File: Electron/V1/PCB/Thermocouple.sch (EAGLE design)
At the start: 30 parts, among them U1 MAX31855K, U2 ELECTRONDUALNAMED, U3 24LC512

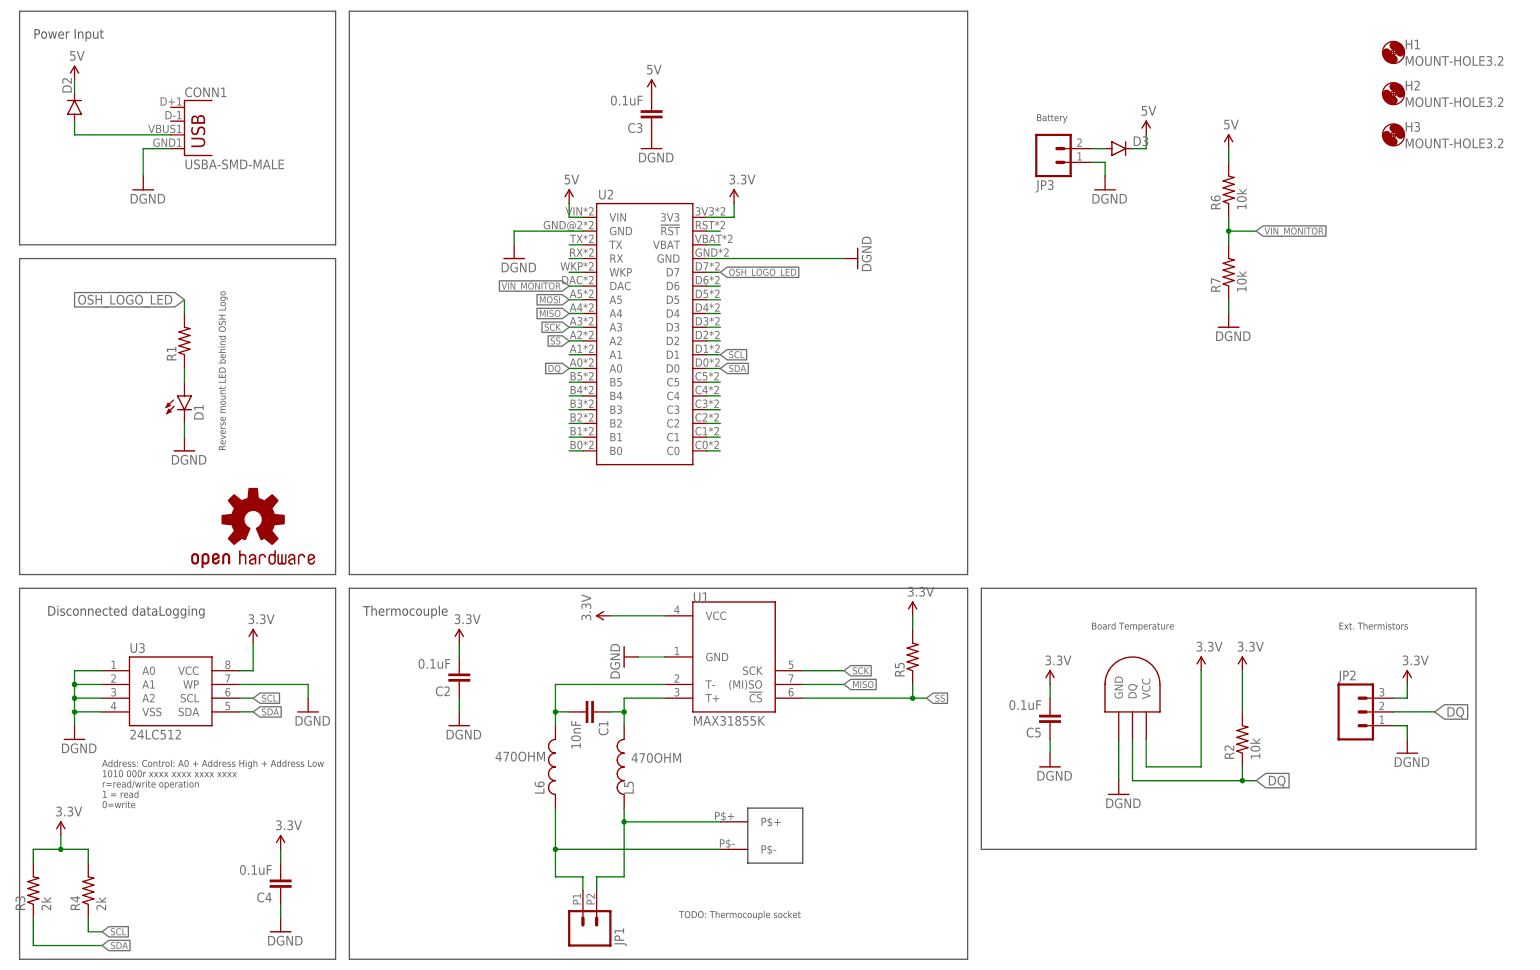
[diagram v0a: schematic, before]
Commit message: Updated to V1.1 * Removed DS18B20 to focus on thermocouple only. * Added solder pads to allow select using A0/1/2 and B0-5 for stackable sensors with single photon/electron. * Removed battery connector and diodes. * Minor change to board dimensions. * Moved OSH Logo + LED down a little for board changes. Added DirtyPCB Images. Added pdfs of PCB/Schematics for V1.1
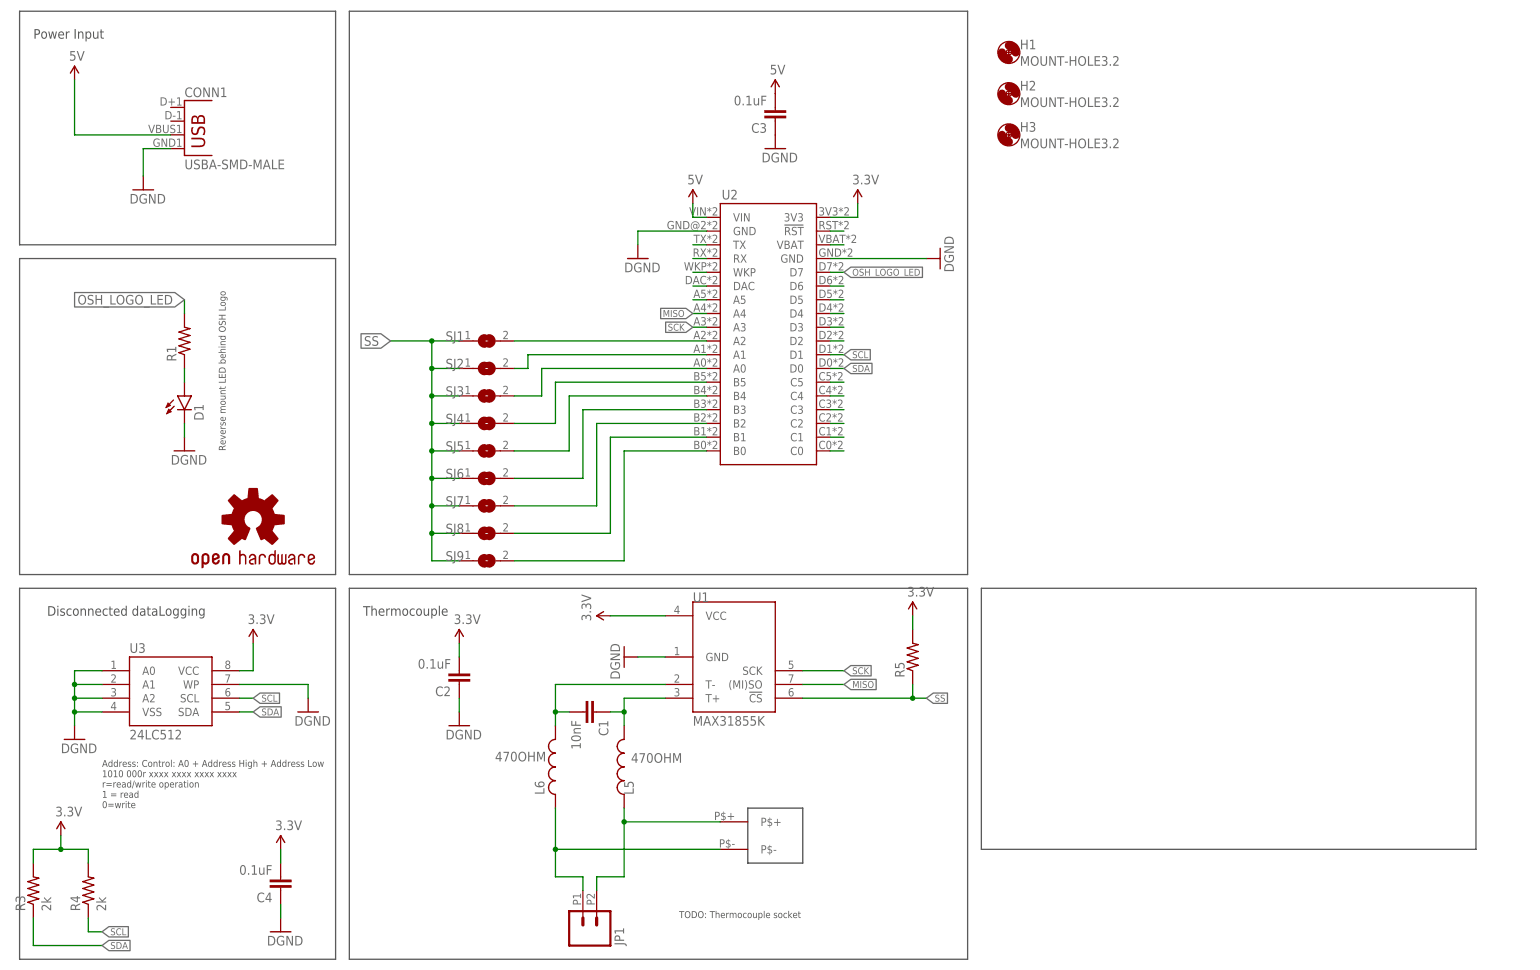
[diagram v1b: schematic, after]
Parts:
- removed C5: 0.1uF, SparkFun-Passives:CAP0805
- removed D2, D3: (no value), SparkFun-DiscreteSemi:DIODESMA
- removed JP2: (no value), SparkFun-Connectors:M03POLAR
- removed JP3: (no value), SparkFun-Connectors:M02-JST-2MM-SMT
- removed R2, R6, R7: 10k, SparkFun-Resistors:RESISTOR0805-RES
- removed U$1: DS1820SOIC, DS1820-SOIC:DS1820SOIC
- added SJ1, SJ2, SJ3, SJ4, SJ5, SJ6, SJ7, SJ8, SJ9: (no value), jumper:SJ
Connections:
- removed net N$1: CONN1.VBUS, D2.A
- removed net VIN_MONITOR: R6.1, R7.2, U2.DAC
- new net N$30: SJ1.2, U2.A2
- net 3.3V: no longer C5.2, JP2.3, R2.2, U$1.VCC
- net 5V: now also CONN1.VBUS; no longer D2.C, D3.C, R6.2
- net DQ: now also SJ3.2; no longer JP2.2, R2.1, U$1.DQ
- net GND: no longer C5.1, JP2.1, JP3.2, R7.1, U$1.GND
- net N$29: now also U2.DAC; no longer D3.A, JP3.1
- net N$3: now also SJ2.2
- net N$31: now also SJ9.2
- net N$33: now also SJ8.2
- net N$35: now also SJ7.2
- net N$36: now also SJ6.2
- net N$37: now also SJ5.2
- net N$38: now also SJ4.2
- net SS: now also SJ1.1, SJ2.1, SJ3.1, SJ4.1, SJ5.1, SJ6.1, SJ7.1, SJ8.1, SJ9.1; no longer U2.A2
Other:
- note removed: "Battery"
- note removed: "Board Temperature"
- note removed: "Ext. Thermistors"
- moved on the sheet: C3, H1, H2, H3, U2

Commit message: Tidied up identifiers and added BOM
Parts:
- R1: value (none) -> 1k5
- R3, R4: value 2k -> 4k7
- R5: value (none) -> 10k
- renumbered U$2 to JP2
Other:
- note added: "Do not fit"
- note added: "Thermocouple socket"
- note removed: "TODO: Thermocouple socket"
- moved on the sheet: C3, H1, H2, H3, SJ1, SJ2, SJ3, SJ4, SJ5, SJ6, SJ7, SJ8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
